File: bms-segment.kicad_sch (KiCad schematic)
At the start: 1 part, among them J1 302-S301

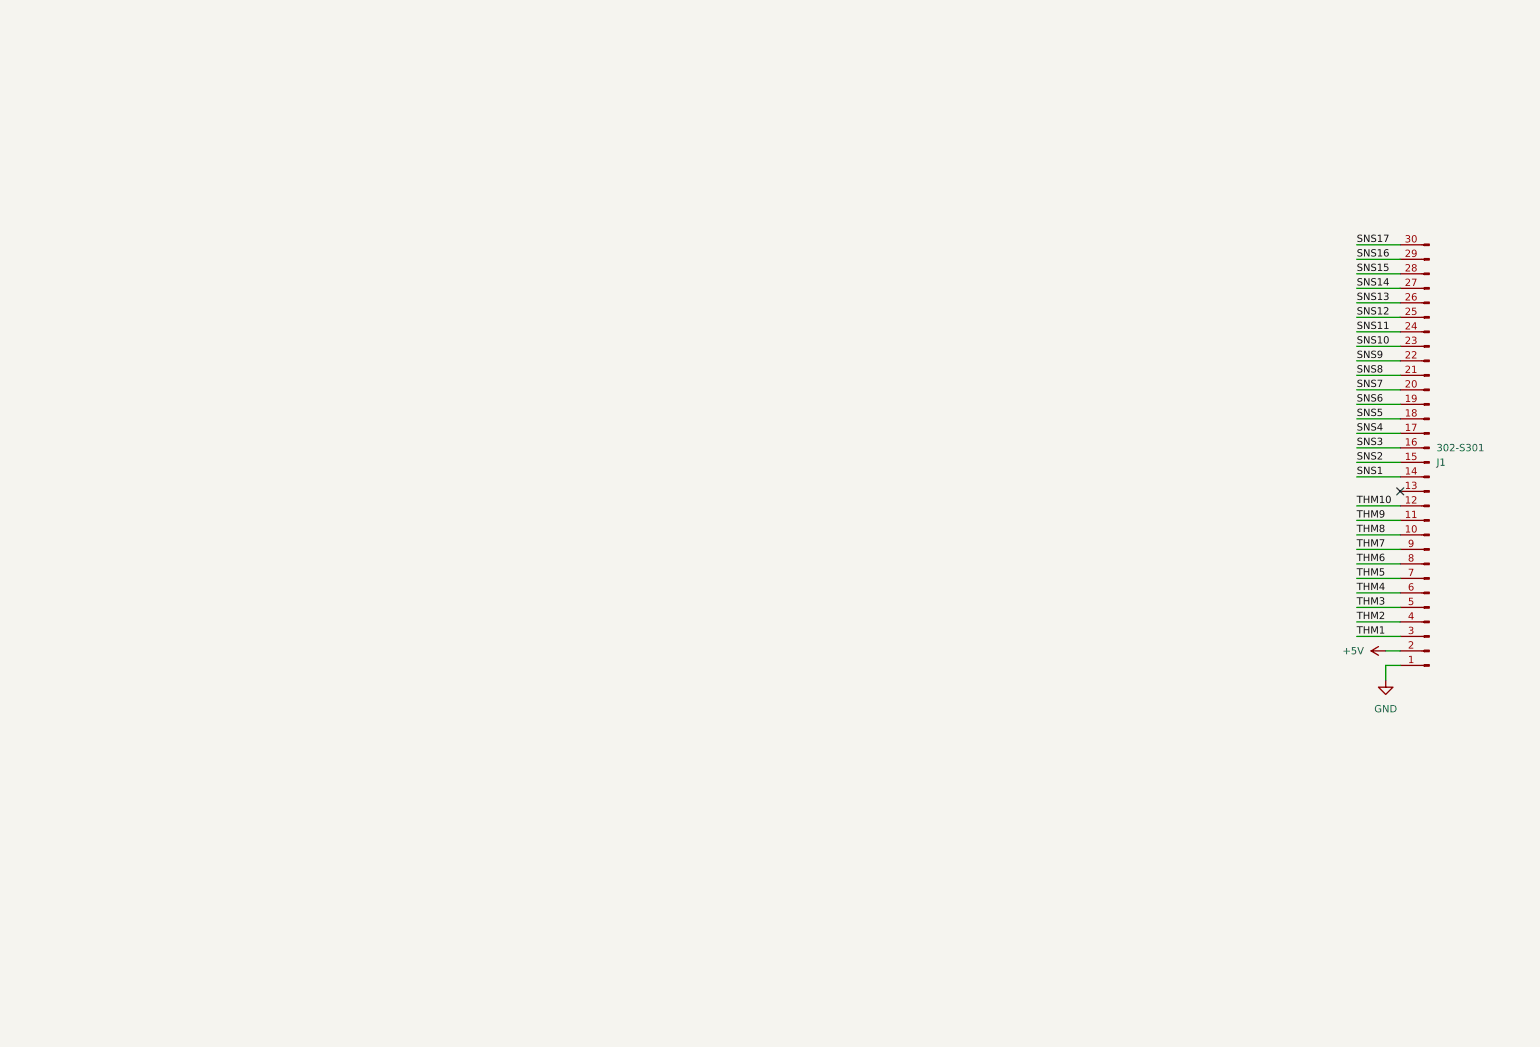
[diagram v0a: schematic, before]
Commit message: Finish schematic draft
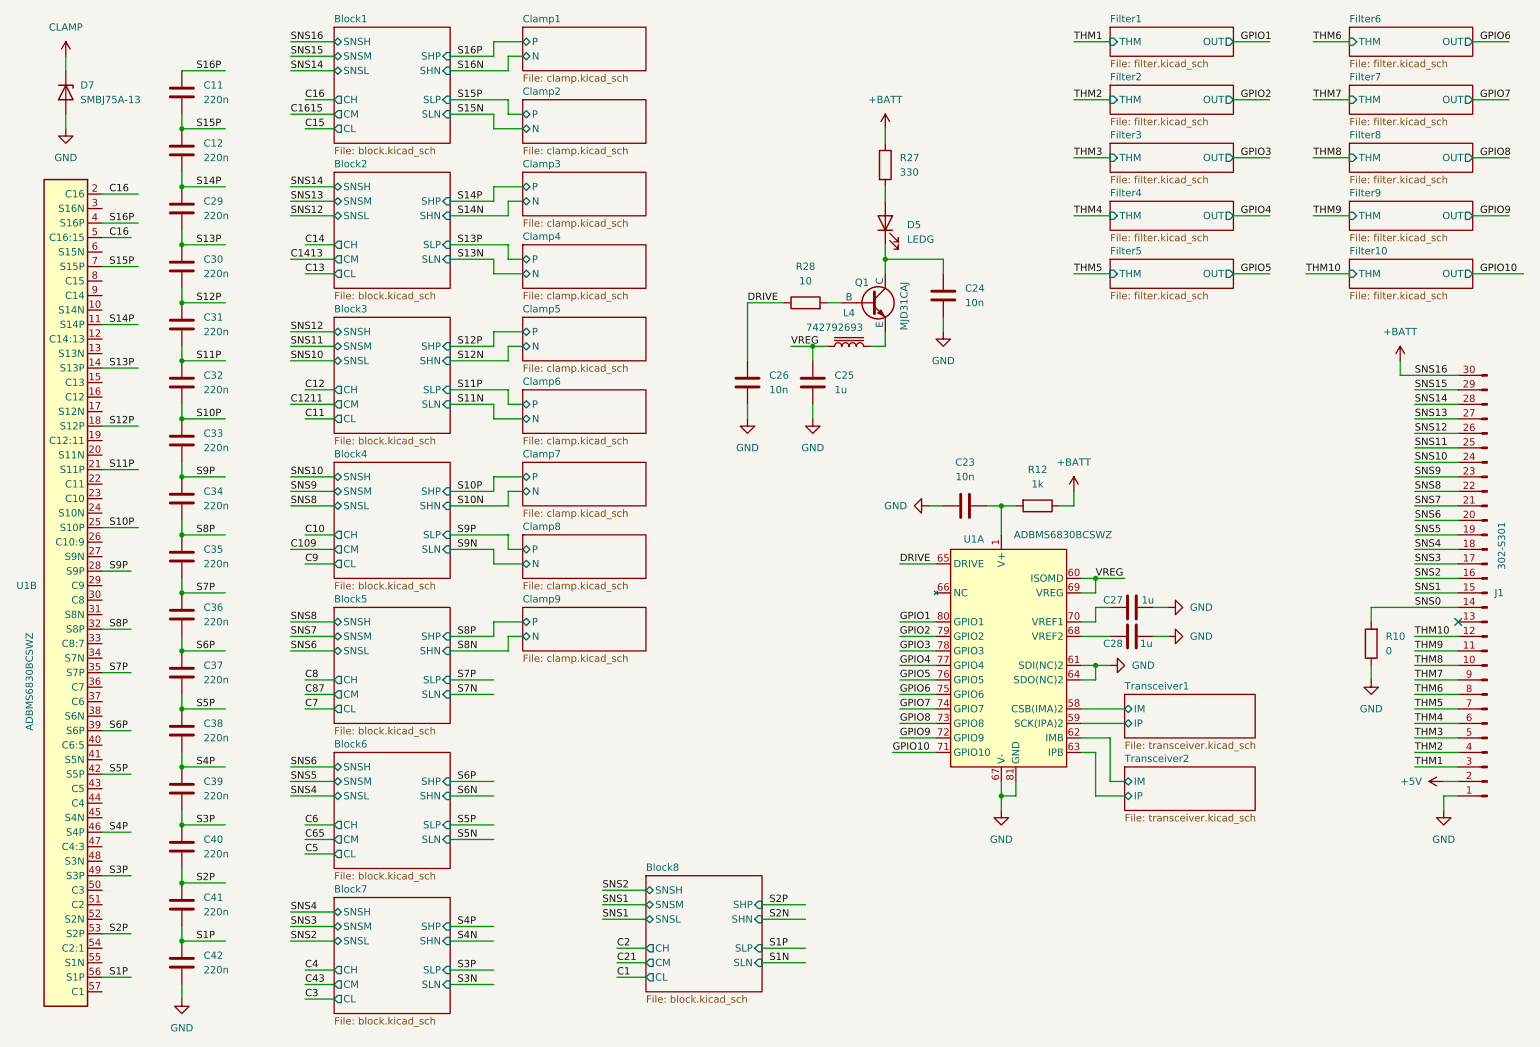
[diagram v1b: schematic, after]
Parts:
- added C11, C12, C29, C30, C31, C32, C33, C34, C35, C36, C37, C38, C39, C40, C41, C42: 220n, symbol Device:C
- added C23, C24, C26: 10n, symbol Device:C
- added C25, C27, C28: 1u, symbol Device:C
- added D5: LEDG, symbol Device:LED
- added D7: SMBJ75A-13, symbol Device:D_Zener
- added L4: 742792693, symbol Device:L_Iron
- added Q1: MJD31CAJ, symbol Simulation_SPICE:NPN
- added R10: 0, symbol Device:R
- added R12: 1k, symbol Device:R
- added R27: 330, symbol Device:R
- added R28: 10, symbol Device:R
- added U1: ADBMS6830BCSWZ, User_Footprints:LQFP-80-1EP_12x12mm_P0.5mm, symbol User_Symbols:ADBMS6830BCSWZ
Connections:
- net SNS16 is gone; now on net SNS15: J1.29 (Pin_29)
- net GND: now also C23.1, C24.2, C25.2, C26.2, C27.2, C28.2, C42.2, D7.2 (A), R10.1, U1.61 (SDI(NC)2), U1.64 (SDO(NC)2), U1.67 (V-), U1.81 (GND)
- net SNS1: now also J1.15 (Pin_15); no longer J1.14 (Pin_14)
- net SNS10: now also J1.24 (Pin_24); no longer J1.23 (Pin_23)
- net SNS11: now also J1.25 (Pin_25); no longer J1.24 (Pin_24)
- net SNS12: now also J1.26 (Pin_26); no longer J1.25 (Pin_25)
- net SNS13: now also J1.27 (Pin_27); no longer J1.26 (Pin_26)
- net SNS14: now also J1.28 (Pin_28); no longer J1.27 (Pin_27)
- net SNS15: no longer J1.28 (Pin_28)
- net SNS2: now also J1.16 (Pin_16); no longer J1.15 (Pin_15)
- net SNS3: now also J1.17 (Pin_17); no longer J1.16 (Pin_16)
- net SNS4: now also J1.18 (Pin_18); no longer J1.17 (Pin_17)
- net SNS5: now also J1.19 (Pin_19); no longer J1.18 (Pin_18)
- net SNS6: now also J1.20 (Pin_20); no longer J1.19 (Pin_19)
- net SNS7: now also J1.21 (Pin_21); no longer J1.20 (Pin_20)
- net SNS8: now also J1.22 (Pin_22); no longer J1.21 (Pin_21)
- net SNS9: now also J1.23 (Pin_23); no longer J1.22 (Pin_22)
- net SNS17 renamed +BATT
- net +BATT: now also R12.1, R27.1
- new net: C24.1, D5.1 (K), Q1.1 (C)
- new net: L4.2, Q1.3 (E)
- new net: Q1.2 (B), R28.2
- new net: C28.1, U1.68 (VREF2)
- new net: D5.2 (A), R27.2
- new net: C23.2, R12.2, U1.1 (V+)
- new net: C27.1, U1.70 (VREF1)
- new net C16: U1.2 (C16), U1.5 (C16:15)
- new net CLAMP: D7.1 (K)
- new net DRIVE: C26.1, R28.1, U1.65 (DRIVE)
- new net GPIO1: U1.80 (GPIO1)
- new net GPIO10: U1.71 (GPIO10)
- new net GPIO2: U1.79 (GPIO2)
- new net GPIO3: U1.78 (GPIO3)
- new net GPIO4: U1.77 (GPIO4)
- new net GPIO5: U1.76 (GPIO5)
- new net GPIO6: U1.75 (GPIO6)
- new net GPIO7: U1.74 (GPIO7)
- new net GPIO8: U1.73 (GPIO8)
- new net GPIO9: U1.72 (GPIO9)
- new net S10P: C32.2, C33.1, U1.25 (S10P)
- new net S11P: C31.2, C32.1, U1.21 (S11P)
- new net S12P: C30.2, C31.1, U1.18 (S12P)
- new net S13P: C29.2, C30.1, U1.14 (S13P)
- new net S14P: C12.2, C29.1, U1.11 (S14P)
- new net S15P: C11.2, C12.1, U1.7 (S15P)
- new net S16P: C11.1, U1.4 (S16P)
- new net S1P: C41.2, C42.1, U1.56 (S1P)
- new net S2P: C40.2, C41.1, U1.53 (S2P)
- new net S3P: C39.2, C40.1, U1.49 (S3P)
- new net S4P: C38.2, C39.1, U1.46 (S4P)
- new net S5P: C37.2, C38.1, U1.42 (S5P)
- new net S6P: C36.2, C37.1, U1.39 (S6P)
- new net S7P: C35.2, C36.1, U1.35 (S7P)
- new net S8P: C34.2, C35.1, U1.32 (S8P)
- new net S9P: C33.2, C34.1, U1.28 (S9P)
- new net SNS0: J1.14 (Pin_14), R10.2
- new net Transceiver1/IM: U1.58 (CSB(IMA)2)
- new net Transceiver1/IP: U1.59 (SCK(IPA)2)
- new net Transceiver2/IM: U1.62 (IMB)
- new net Transceiver2/IP: U1.63 (IPB)
- new net VREG: C25.1, L4.1, U1.60 (ISOMD), U1.69 (VREG)
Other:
- added sheet Block1 (block.kicad_sch)
- added sheet Block2 (block.kicad_sch)
- added sheet Block3 (block.kicad_sch)
- added sheet Block4 (block.kicad_sch)
- added sheet Block5 (block.kicad_sch)
- added sheet Block6 (block.kicad_sch)
- added sheet Block7 (block.kicad_sch)
- added sheet Block8 (block.kicad_sch)
- added sheet Clamp1 (clamp.kicad_sch)
- added sheet Clamp2 (clamp.kicad_sch)
- added sheet Clamp3 (clamp.kicad_sch)
- added sheet Clamp4 (clamp.kicad_sch)
- added sheet Clamp5 (clamp.kicad_sch)
- added sheet Clamp6 (clamp.kicad_sch)
- added sheet Clamp7 (clamp.kicad_sch)
- added sheet Clamp8 (clamp.kicad_sch)
- added sheet Clamp9 (clamp.kicad_sch)
- added sheet Filter1 (filter.kicad_sch)
- added sheet Filter10 (filter.kicad_sch)
- added sheet Filter2 (filter.kicad_sch)
- added sheet Filter3 (filter.kicad_sch)
- added sheet Filter4 (filter.kicad_sch)
- added sheet Filter5 (filter.kicad_sch)
- added sheet Filter6 (filter.kicad_sch)
- added sheet Filter7 (filter.kicad_sch)
- added sheet Filter8 (filter.kicad_sch)
- added sheet Filter9 (filter.kicad_sch)
- added sheet Transceiver1 (transceiver.kicad_sch)
- added sheet Transceiver2 (transceiver.kicad_sch)
- moved on the sheet: J1

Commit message: Save progress
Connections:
- net +5V is gone; now on net VREG: J1.2 (Pin_2)
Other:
- note added: "(5V)"
- moved on the sheet: J1, R10
